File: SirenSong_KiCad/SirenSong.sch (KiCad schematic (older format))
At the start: 17 parts

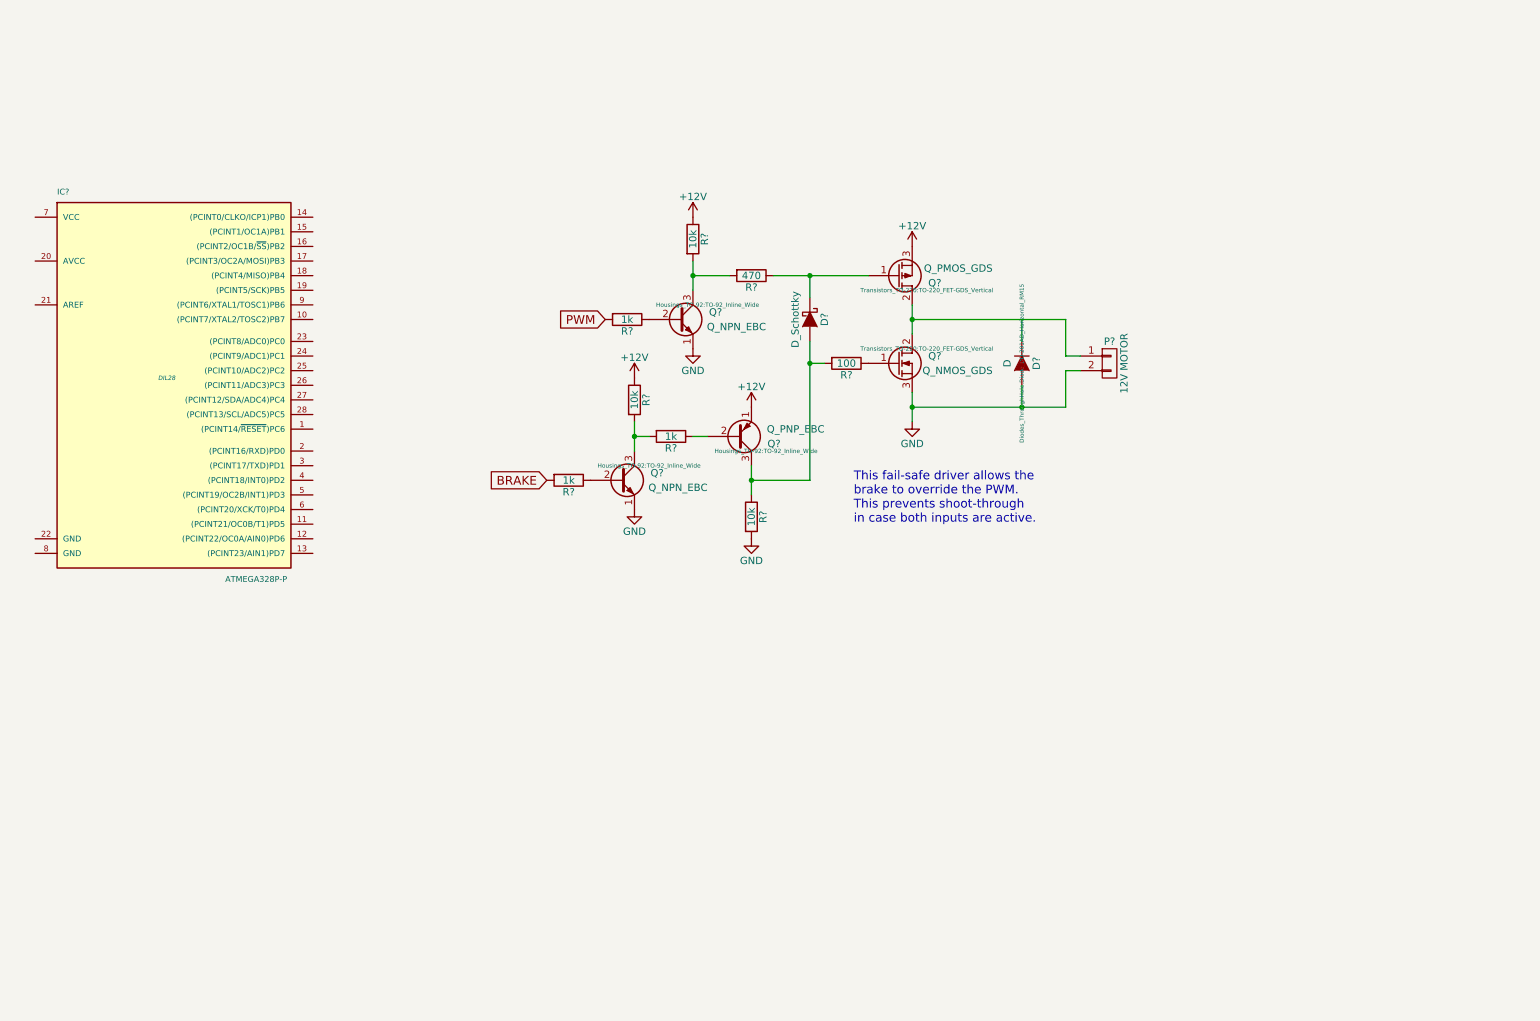
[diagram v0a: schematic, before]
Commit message: As-built Schematic
Completed the KiCad schematic, with documentation.
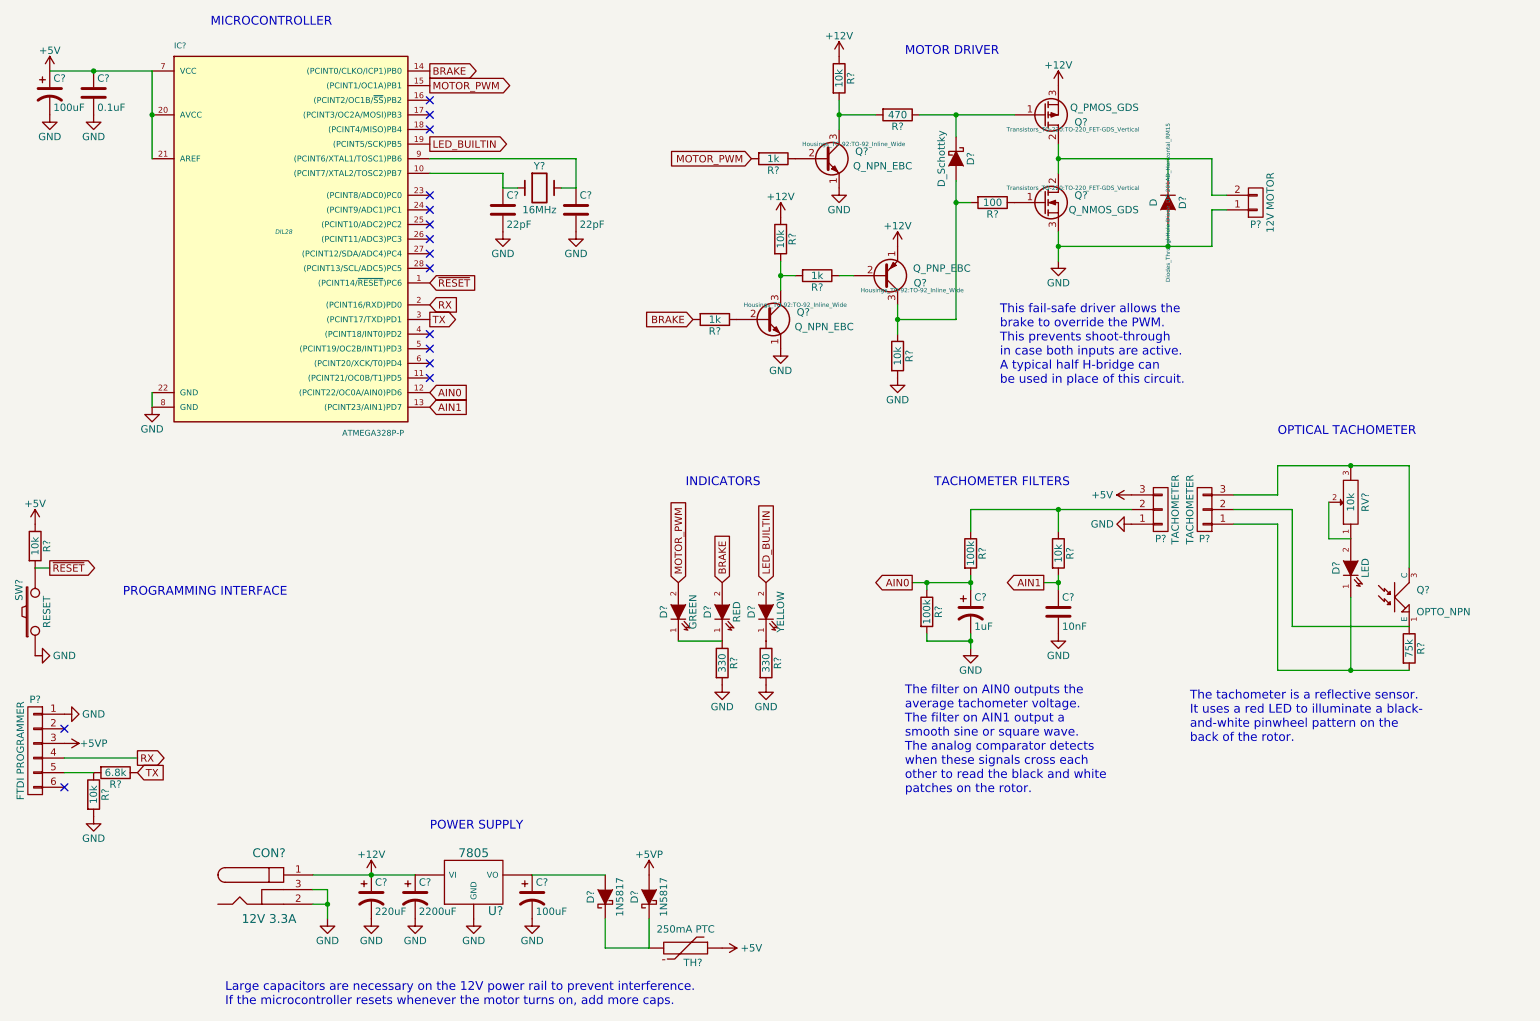
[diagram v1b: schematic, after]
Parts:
- added C?: 10nF, symbol C
- added C?: 1uF, symbol CP1
- added C? (x2): 100uF, symbol CP1
- added C?: 2200uF, symbol CP1
- added C?: 220uF, symbol CP1
- added C?: 0.1uF, symbol C
- added C? (x2): 22pF, symbol C
- added CON?: 12V 3.3A, symbol BARREL_JACK
- added D?: GREEN, symbol LED
- added D?: RED, symbol LED
- added D?: YELLOW, symbol LED
- added D? (x2): 1N5817, symbol D_Schottky
- added D?: LED, symbol LED
- added P? (x2): TACHOMETER, symbol CONN_01X03
- added P?: FTDI PROGRAMMER, symbol CONN_01X06
- added Q?: OPTO_NPN, symbol OPTO_NPN
- added R? (x3): 10k, symbol R
- added R? (x2): 100k, symbol R
- added R? (x2): 330, symbol R
- added R?: 6.8k, symbol R
- added R?: 75k, symbol R
- added RV?: 10k, symbol POT
- added SW?: RESET, symbol SW_PUSH
- added TH?: 250mA PTC, symbol THERMISTOR
- added U?: 7805, symbol 7805
- added Y?: 16MHz, symbol Crystal
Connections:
- net labels added: +5V, +5VP, AIN0, AIN1, LED_BUILTIN, MOTOR_PWM, RX, TX, ~RESET
- net labels removed: PWM
- wire segments 29 -> 85
- no-connect marks 0 -> 15
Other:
- note added: "INDICATORS"
- note added: "Large capacitors are necessary on the 12V power rail to prevent interference.\nIf the microcontroller resets whenever the motor turns on, add more caps."
- note added: "MICROCONTROLLER"
- note added: "MOTOR DRIVER"
- note added: "OPTICAL TACHOMETER"
- note added: "POWER SUPPLY"
- note added: "PROGRAMMING INTERFACE"
- note added: "TACHOMETER FILTERS"
- note added: "The filter on AIN0 outputs the\naverage tachometer voltage.\nThe filter on AIN1 output a\nsmooth sine or square wave.\nThe analog comparator detects\nwhen these signals cross each\nother to read the black and white\npatches on the rotor."
- note added: "The tachometer is a reflective sensor.\nIt uses a red LED to illuminate a black-\nand-white pinwheel pattern on the\nback of the rotor."
- note added: "This fail-safe driver allows the\nbrake to override the PWM.\nThis prevents shoot-through\nin case both inputs are active.\nA typical half H-bridge can\nbe used in place of this circuit."
- note removed: "This fail-safe driver allows the\nbrake to override the PWM.\nThis prevents shoot-through\nin case both inputs are active."
- moved on the sheet: D?, IC?, P?, Q?, R?

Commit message: Schematic Image
Added screen capture of the entire schematic, for those who don't have KiCad.
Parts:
- CON?: value 12V 3.3A -> J1
- Q3, Q5: renamed from Q?; value Q_NPN_EBC -> 2N3904
- Q4: renamed from Q?; value Q_PNP_EBC -> 2N3905
- Q6: renamed from Q?; value OPTO_NPN -> ALS-PT204-6C/L177
- TB1: renamed from P?; value 12V MOTOR -> SIREN MOTOR
- gave numbers to parts that had none: 15
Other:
- moved on the sheet: C6, C7, D?, J3, P3, Q6, R?, RV?

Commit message: Fixed resistor value
Changed incorrect bleeder resistor value on C6.
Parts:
- R?: value 100k -> 1M
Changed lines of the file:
@@
 P 6700 5000
 F 0 "R?" V 6780 5000 50  0000 C CNN
-F 1 "100k" V 6700 5000 50  0000 C CNN
+F 1 "1M" V 6700 5000 50  0000 C CNN
 F 2 "" V 6630 5000 30  0000 C CNN
 F 3 "" H 6700 5000 30  0000 C CNN
